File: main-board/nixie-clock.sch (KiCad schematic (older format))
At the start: 28 parts, among them P1 ESP8266_CONN, P2 CONN_01X06, Q2 Q_NMOS_DGS, Q3 Q_NMOS_DGS, SW1 ROTARY_ENCODER_SWITCH, U1 STM32F103CBT6, Y1 32.768kHz

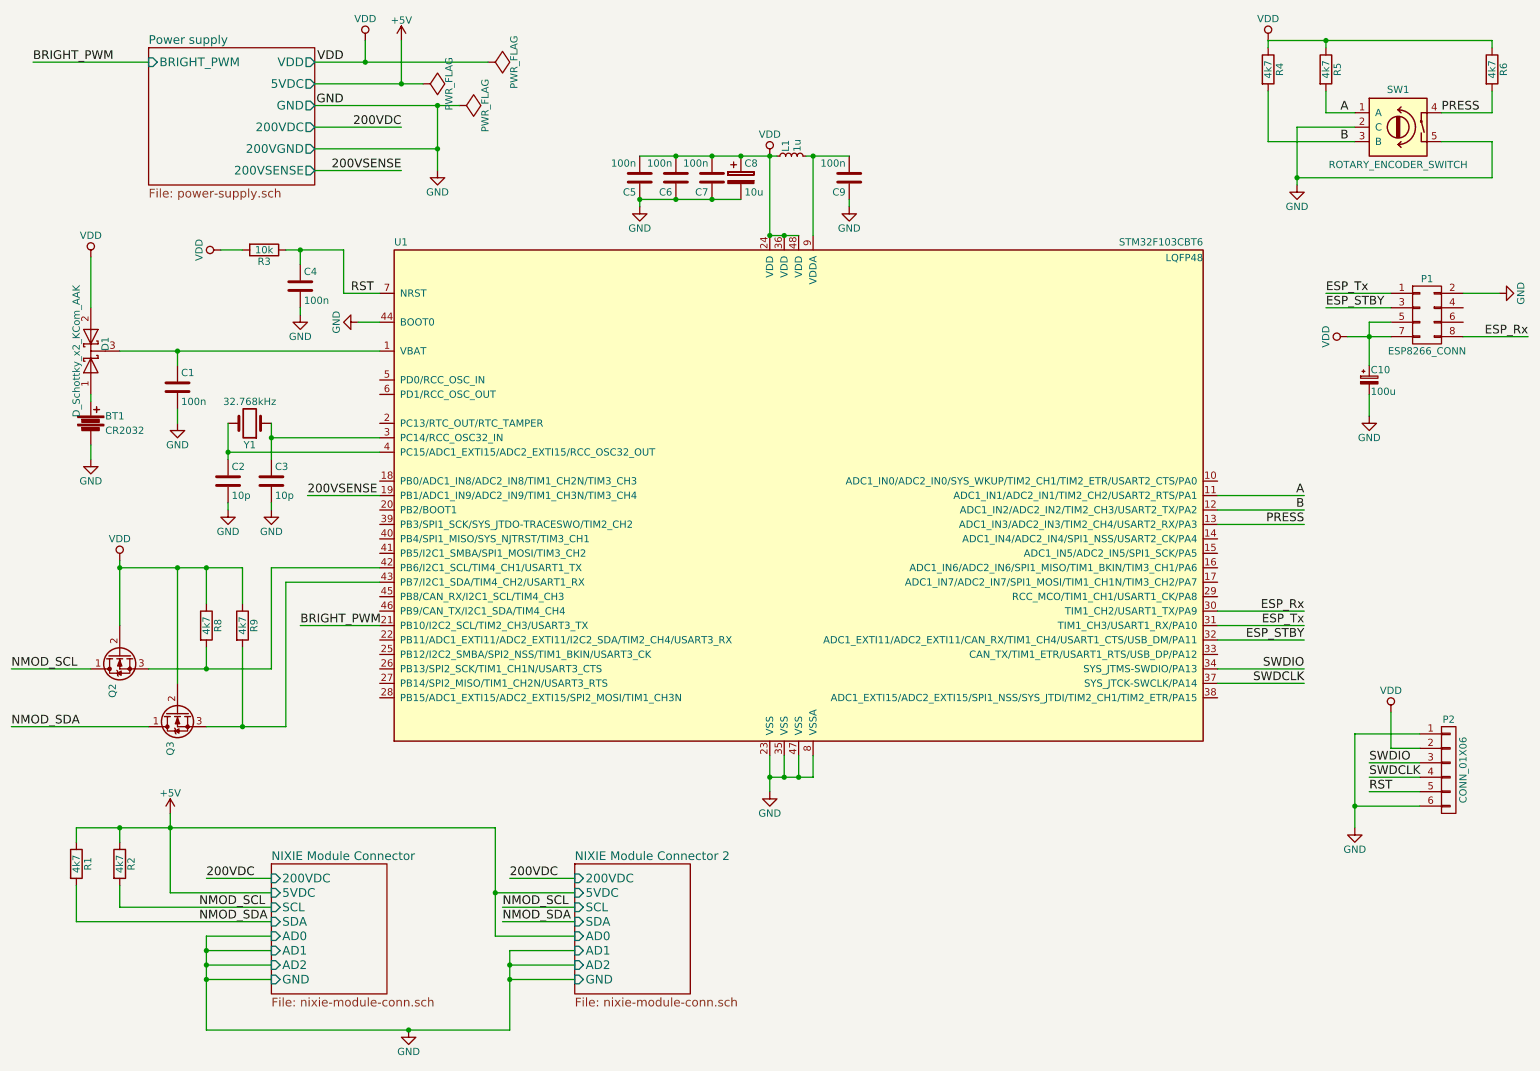
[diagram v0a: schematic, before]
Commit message: Oznaczenie MOSFET-ow od I2C; pojemnosc do filtrowania wysokich czestotliwosci za przetwornica boost; obudowy wiekszosci elementow
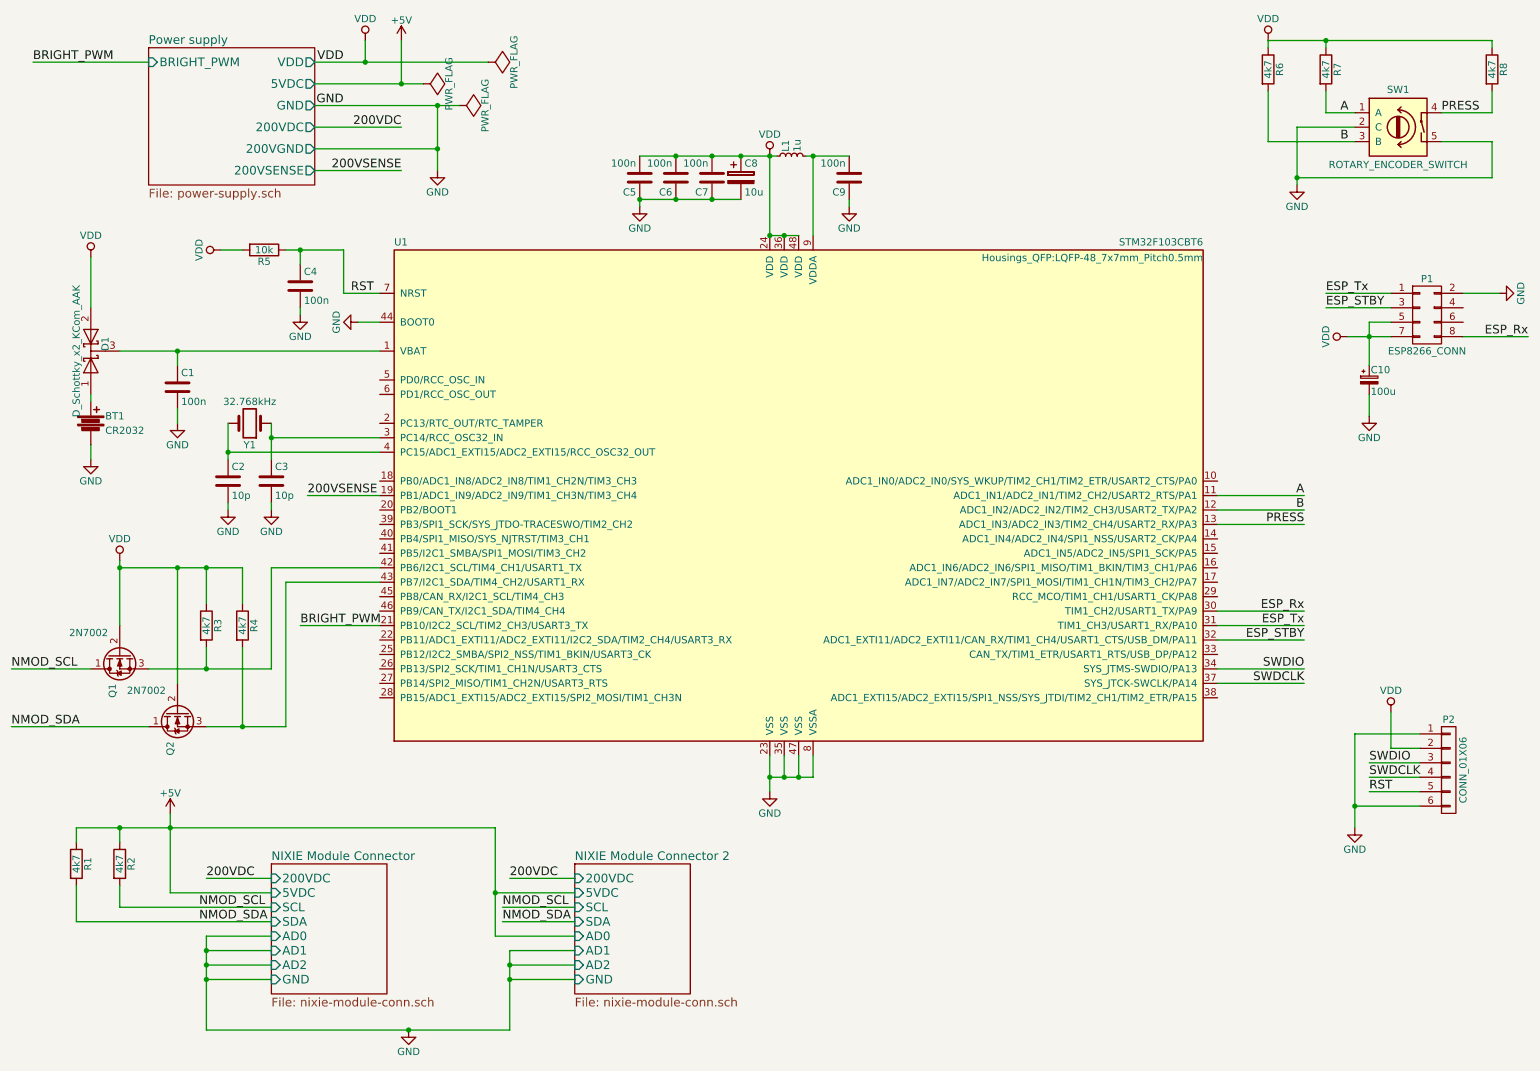
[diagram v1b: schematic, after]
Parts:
- BT1: footprint (none) -> Connect:CR2032H
- C1, C2, C3, C4, C5, C6, C7, C9: footprint (none) -> Capacitors_SMD:C_0805_HandSoldering
- C10: footprint (none) -> Capacitors_Tantalum_SMD:TantalC_SizeC_EIA-6032_HandSoldering
- C8: footprint (none) -> Capacitors_Tantalum_SMD:TantalC_SizeB_EIA-3528_HandSoldering
- D1: footprint (none) -> TO_SOT_Packages_SMD:SOT-23_Handsoldering
- L1: footprint (none) -> Choke_SMD:Choke_SMD_1206_Handsoldering
- P1: footprint (none) -> Pin_Headers:Pin_Header_Straight_SMT_02x04
- P2, SW1: footprint (none) -> Pin_Headers:Pin_Header_Straight_SMT_02x03
- Q1: renamed from Q2; value Q_NMOS_DGS -> 2N7002; footprint (none) -> TO_SOT_Packages_SMD:SOT-23_Handsoldering
- Q2: renamed from Q3; value Q_NMOS_DGS -> 2N7002; footprint (none) -> TO_SOT_Packages_SMD:SOT-23_Handsoldering
- R1, R2: footprint (none) -> Resistors_SMD:R_0805_HandSoldering
- R3: renamed from R8; footprint (none) -> Resistors_SMD:R_0805_HandSoldering
- R4: renamed from R9; footprint (none) -> Resistors_SMD:R_0805_HandSoldering
- R5: renamed from R3; footprint (none) -> Resistors_SMD:R_0805_HandSoldering
- R6: renamed from R4; footprint (none) -> Resistors_SMD:R_0805_HandSoldering
- R7: renamed from R5; footprint (none) -> Resistors_SMD:R_0805_HandSoldering
- R8: renamed from R6; footprint (none) -> Resistors_SMD:R_0805_HandSoldering
- U1: footprint LQFP48 -> Housings_QFP:LQFP-48_7x7mm_Pitch0.5mm
- Y1: footprint (none) -> Crystals:Crystal_Round_Vertical_3mm_BigPad
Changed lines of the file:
@@
 F 0 "U1" H 3200 5575 50  0000 L BNN
 F 1 "STM32F103CBT6" H 8800 5575 50  0000 R BNN
-F 2 "LQFP48" H 8800 5525 50  0000 R TNN
+F 2 "Housings_QFP:LQFP-48_7x7mm_Pitch0.5mm" H 8800 5525 50  0000 R TNN
 F 3 "" H 6000 3850 50  0000 C CNN
 	1    6000 3850
@@
 F 0 "Y1" H 2200 3500 50  0000 C CNN
 F 1 "32.768kHz" H 2200 3200 50  0000 C CNN
-F 2 "" H 2200 3350 50  0000 C CNN
+F 2 "Crystals:Crystal_Round_Vertical_3mm_BigPad" H 2200 3350 50  0001 C CNN
 F 3 "" H 2200 3350 50  0000 C CNN
 F 4 "LFXTAL002996BULK" H 2200 3350 60  0001 C CNN "Part no."
@@
 F 0 "C2" H 2075 3850 50  0000 L CNN
 F 1 "10p" H 2075 3650 50  0000 L CNN
-F 2 "" H 2088 3600 50  0000 C CNN
+F 2 "Capacitors_SMD:C_0805_HandSoldering" H 2088 3600 50  0001 C CNN
 F 3 "" H 2050 3750 50  0000 C CNN
 	1    2050 3750
@@
 F 0 "C3" H 2375 3850 50  0000 L CNN
 F 1 "10p" H 2375 3650 50  0000 L CNN
-F 2 "" H 2388 3600 50  0000 C CNN
+F 2 "Capacitors_SMD:C_0805_HandSoldering" H 2388 3600 50  0001 C CNN
 F 3 "" H 2350 3750 50  0000 C CNN
 	1    2350 3750
@@
 F 0 "D1" H 1150 2750 50  0000 C CNN
 F 1 "D_Schottky_x2_KCom_AAK" H 1100 2950 50  0000 C CNN
-F 2 "" H 1100 2850 50  0000 C CNN
+F 2 "TO_SOT_Packages_SMD:SOT-23_Handsoldering" H 1100 2850 50  0001 C CNN
 F 3 "" H 1100 2850 50  0000 C CNN
 	1    1100 2850
@@
 F 0 "C1" H 1725 3200 50  0000 L CNN
 F 1 "100n" H 1725 3000 50  0000 L CNN
-F 2 "" H 1738 2950 50  0000 C CNN
+F 2 "Capacitors_SMD:C_0805_HandSoldering" H 1738 2950 50  0001 C CNN
 F 3 "" H 1700 3100 50  0000 C CNN
 	1    1700 3100
@@
 F 0 "BT1" H 1200 3400 50  0000 L CNN
 F 1 "CR2032" H 1200 3300 50  0000 L CNN
-F 2 "" V 1100 3390 50  0000 C CNN
+F 2 "Connect:CR2032H" V 1100 3390 50  0001 C CNN
 F 3 "" V 1100 3390 50  0000 C CNN
 	1    1100 3350
@@
 F 0 "P1" H 10350 2850 50  0000 C CNN
 F 1 "ESP8266_CONN" H 10350 2350 50  0000 C CNN
-F 2 "" H 10350 1400 50  0000 C CNN
+F 2 "Pin_Headers:Pin_Header_Straight_SMT_02x04" H 10350 1400 50  0001 C CNN
 F 3 "" H 10350 1400 50  0000 C CNN
 	1    10350 2600
@@
 F 0 "R2" V 1380 6400 50  0000 C CNN
 F 1 "4k7" V 1300 6400 50  0000 C CNN
-F 2 "" V 1230 6400 50  0000 C CNN
+F 2 "Resistors_SMD:R_0805_HandSoldering" V 1230 6400 50  0001 C CNN
 F 3 "" H 1300 6400 50  0000 C CNN
 	1    1300 6400
@@
 F 0 "R1" V 1080 6400 50  0000 C CNN
 F 1 "4k7" V 1000 6400 50  0000 C CNN
-F 2 "" V 930 6400 50  0000 C CNN
+F 2 "Resistors_SMD:R_0805_HandSoldering" V 930 6400 50  0001 C CNN
 F 3 "" H 1000 6400 50  0000 C CNN
 	1    1000 6400
@@
 F 0 "L1" H 5980 1540 50  0000 L CNN
 F 1 "1u" H 5980 1460 50  0000 L CNN
-F 2 "" H 5950 1500 50  0000 C CNN
+F 2 "Choke_SMD:Choke_SMD_1206_Handsoldering" H 5950 1500 50  0001 C CNN
 F 3 "" H 5950 1500 50  0000 C CNN
 	1    5950 1500
@@
 F 0 "C5" H 4925 1750 50  0000 L CNN
 F 1 "100n" H 4925 1550 50  0000 L CNN
-F 2 "" H 4938 1500 50  0000 C CNN
+F 2 "Capacitors_SMD:C_0805_HandSoldering" H 4938 1500 50  0001 C CNN
 F 3 "" H 4900 1650 50  0000 C CNN
 	1    4900 1650
@@
 F 0 "C6" H 5175 1750 50  0000 L CNN
 F 1 "100n" H 5175 1550 50  0000 L CNN
-F 2 "" H 5188 1500 50  0000 C CNN
+F 2 "Capacitors_SMD:C_0805_HandSoldering" H 5188 1500 50  0001 C CNN
 F 3 "" H 5150 1650 50  0000 C CNN
 	1    5150 1650
@@
 F 0 "C7" H 5425 1750 50  0000 L CNN
 F 1 "100n" H 5425 1550 50  0000 L CNN
-F 2 "" H 5438 1500 50  0000 C CNN
+F 2 "Capacitors_SMD:C_0805_HandSoldering" H 5438 1500 50  0001 C CNN
 F 3 "" H 5400 1650 50  0000 C CNN
 	1    5400 1650
@@
 F 0 "C9" H 6375 1750 50  0000 L CNN
 F 1 "100n" H 6375 1550 50  0000 L CNN
-F 2 "" H 6388 1500 50  0000 C CNN
+F 2 "Capacitors_SMD:C_0805_HandSoldering" H 6388 1500 50  0001 C CNN
 F 3 "" H 6350 1650 50  0000 C CNN
 	1    6350 1650
@@
 F 0 "C8" H 5625 1750 50  0000 L CNN
 F 1 "10u" H 5625 1550 50  0000 L CNN
-F 2 "" H 5638 1500 50  0000 C CNN
+F 2 "Capacitors_Tantalum_SMD:TantalC_SizeB_EIA-3528_HandSoldering" H 5638 1500 50  0001 C CNN
 F 3 "" H 5600 1650 50  0000 C CNN
 	1    5600 1650
@@
 F 0 "C10" H 9960 3120 50  0000 L CNN
 F 1 "100u" H 9960 2970 50  0000 L CNN
-F 2 "" H 9950 3050 50  0000 C CNN
+F 2 "Capacitors_Tantalum_SMD:TantalC_SizeC_EIA-6032_HandSoldering" H 9950 3050 50  0001 C CNN
 F 3 "" H 9950 3050 50  0000 C CNN
 	1    9950 3050
@@
 F 0 "SW1" H 10150 1560 50  0000 C CNN
 F 1 "ROTARY_ENCODER_SWITCH" H 10150 1040 50  0000 C CNN
-F 2 "" H 10050 1460 50  0001 C CNN
+F 2 "Pin_Headers:Pin_Header_Straight_SMT_02x03" H 10050 1460 50  0001 C CNN
 F 3 "" H 10150 1560 50  0001 C CNN
 	1    10150 1300
@@
 	9450 1300 9450 1700
 $Comp
-L R R5
+L R R7
 U 1 1 58287760
 P 9650 900
-F 0 "R5" V 9730 900 50  0000 C CNN
+F 0 "R7" V 9730 900 50  0000 C CNN
 F 1 "4k7" V 9650 900 50  0000 C CNN
-F 2 "" V 9580 900 50  0000 C CNN
+F 2 "Resistors_SMD:R_0805_HandSoldering" V 9580 900 50  0001 C CNN
 F 3 "" H 9650 900 50  0000 C CNN
 	1    9650 900
@@
 $EndComp
 $Comp
-L R R4
+L R R6
 U 1 1 58289107
 P 9250 900
-F 0 "R4" V 9330 900 50  0000 C CNN
+F 0 "R6" V 9330 900 50  0000 C CNN
 F 1 "4k7" V 9250 900 50  0000 C CNN
-F 2 "" V 9180 900 50  0000 C CNN
+F 2 "Resistors_SMD:R_0805_HandSoldering" V 9180 900 50  0001 C CNN
 F 3 "" H 9250 900 50  0000 C CNN
 	1    9250 900
@@
 B
 $Comp
-L R R6
+L R R8
 U 1 1 5829021F
 P 10800 900
-F 0 "R6" V 10880 900 50  0000 C CNN
+F 0 "R8" V 10880 900 50  0000 C CNN
 F 1 "4k7" V 10800 900 50  0000 C CNN
-F 2 "" V 10730 900 50  0000 C CNN
+F 2 "Resistors_SMD:R_0805_HandSoldering" V 10730 900 50  0001 C CNN
 F 3 "" H 10800 900 50  0000 C CNN
 	1    10800 900
@@
 F 0 "P2" H 10500 6100 50  0000 C CNN
 F 1 "CONN_01X06" V 10600 5750 50  0000 C CNN
-F 2 "" H 10500 5750 50  0000 C CNN
+F 2 "Pin_Headers:Pin_Header_Straight_SMT_02x03" H 10500 5750 50  0001 C CNN
 F 3 "" H 10500 5750 50  0000 C CNN
 	1    10500 5750
@@
 F 0 "C4" H 2575 2500 50  0000 L CNN
 F 1 "100n" H 2575 2300 50  0000 L CNN
-F 2 "" H 2588 2250 50  0000 C CNN
+F 2 "Capacitors_SMD:C_0805_HandSoldering" H 2588 2250 50  0001 C CNN
 F 3 "" H 2550 2400 50  0000 C CNN
 	1    2550 2400
@@
 $EndComp
 $Comp
-L R R3
+L R R5
 U 1 1 582A7E8D
 P 2300 2150
-F 0 "R3" V 2380 2150 50  0000 C CNN
+F 0 "R5" V 2380 2150 50  0000 C CNN
 F 1 "10k" V 2300 2150 50  0000 C CNN
-F 2 "" V 2230 2150 50  0000 C CNN
+F 2 "Resistors_SMD:R_0805_HandSoldering" V 2230 2150 50  0001 C CNN
 F 3 "" H 2300 2150 50  0000 C CNN
 	1    2300 2150
@@
 	2550 4750 3100 4750
 $Comp
-L VDD #PWR?
+L VDD #PWR028
 U 1 1 58311767
 P 1300 4300
-F 0 "#PWR?" H 1300 4150 50  0001 C CNN
+F 0 "#PWR028" H 1300 4150 50  0001 C CNN
 F 1 "VDD" H 1300 4450 50  0000 C CNN
 F 2 "" H 1300 4300 50  0000 C CNN
@@
 $EndComp
 $Comp
-L Q_NMOS_DGS Q2
+L Q_NMOS_DGS Q1
 U 1 1 583161E1
 P 1300 4950
-F 0 "Q2" H 1600 5000 50  0000 R CNN
-F 1 "Q_NMOS_DGS" H 1950 4900 50  0001 R CNN
-F 2 "" H 1500 5050 50  0000 C CNN
+F 0 "Q1" H 1600 5000 50  0000 R CNN
+F 1 "2N7002" V 1150 5300 50  0000 R CNN
+F 2 "TO_SOT_Packages_SMD:SOT-23_Handsoldering" H 1500 5050 50  0001 C CNN
 F 3 "" H 1300 4950 50  0000 C CNN
 	1    1300 4950
@@
 $EndComp
 $Comp
-L Q_NMOS_DGS Q3
+L Q_NMOS_DGS Q2
 U 1 1 583163F0
 P 1700 5350
-F 0 "Q3" H 2000 5400 50  0000 R CNN
-F 1 "Q_NMOS_DGS" H 2350 5300 50  0001 R CNN
-F 2 "" H 1900 5450 50  0000 C CNN
+F 0 "Q2" H 2000 5400 50  0000 R CNN
+F 1 "2N7002" V 1550 5700 50  0000 R CNN
+F 2 "TO_SOT_Packages_SMD:SOT-23_Handsoldering" H 1900 5450 50  0001 C CNN
 F 3 "" H 1700 5350 50  0000 C CNN
 	1    1700 5350
@@
 	550  5450 1500 5450
 $Comp
-L R R8
+L R R3
 U 1 1 58316CD4
 P 1900 4750
-F 0 "R8" V 1980 4750 50  0000 C CNN
+F 0 "R3" V 1980 4750 50  0000 C CNN
 F 1 "4k7" V 1900 4750 50  0000 C CNN
-F 2 "" V 1830 4750 50  0000 C CNN
+F 2 "Resistors_SMD:R_0805_HandSoldering" V 1830 4750 50  0001 C CNN
 F 3 "" H 1900 4750 50  0000 C CNN
 	1    1900 4750
@@
 $EndComp
 $Comp
-L R R9
+L R R4
 U 1 1 58316DFA
 P 2150 4750
-F 0 "R9" V 2230 4750 50  0000 C CNN
+F 0 "R4" V 2230 4750 50  0000 C CNN
 F 1 "4k7" V 2150 4750 50  0000 C CNN
-F 2 "" V 2080 4750 50  0000 C CNN
+F 2 "Resistors_SMD:R_0805_HandSoldering" V 2080 4750 50  0001 C CNN
 F 3 "" H 2150 4750 50  0000 C CNN
 	1    2150 4750

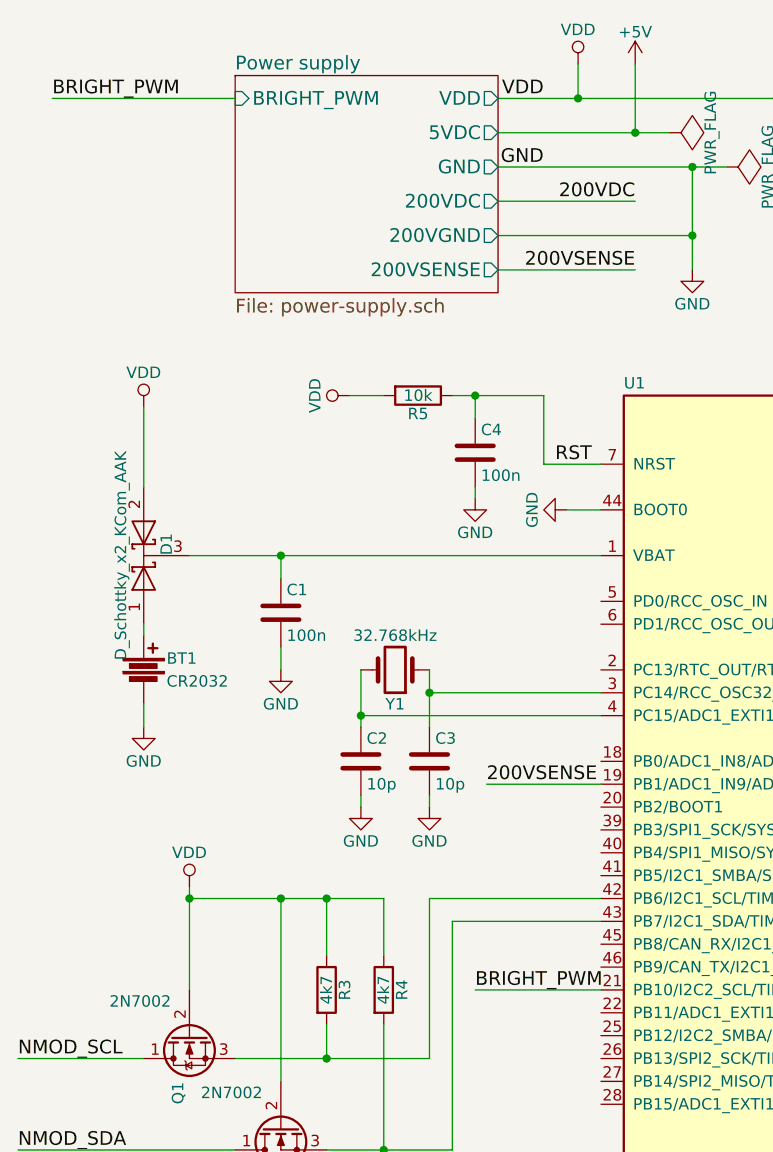
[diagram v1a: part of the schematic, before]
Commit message: Poprawione polaczenie sciezek; zmiana nazwy wyjscia VDD
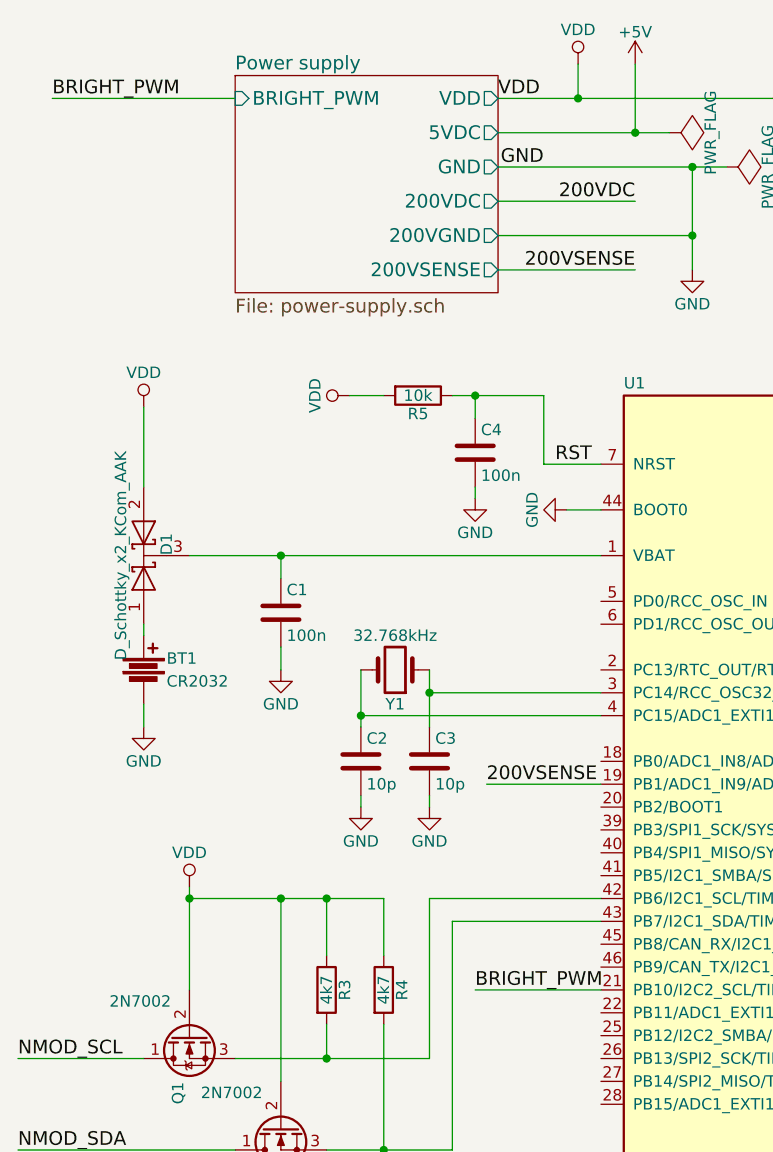
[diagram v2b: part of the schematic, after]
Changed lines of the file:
@@
 Wire Wire Line
 	2650 850  3850 850
-Text Label 2850 850  2    60   ~ 0
+Text Label 2650 850  0    60   ~ 0
 VDD
 Text Label 2850 1150 2    60   ~ 0
@@
 $EndComp
 Wire Wire Line
-	1300 4750 1300 4300
+	1300 4300 1300 4750
 Wire Wire Line
 	1700 5150 1700 4350
